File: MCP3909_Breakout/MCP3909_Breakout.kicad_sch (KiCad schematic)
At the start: 1 part

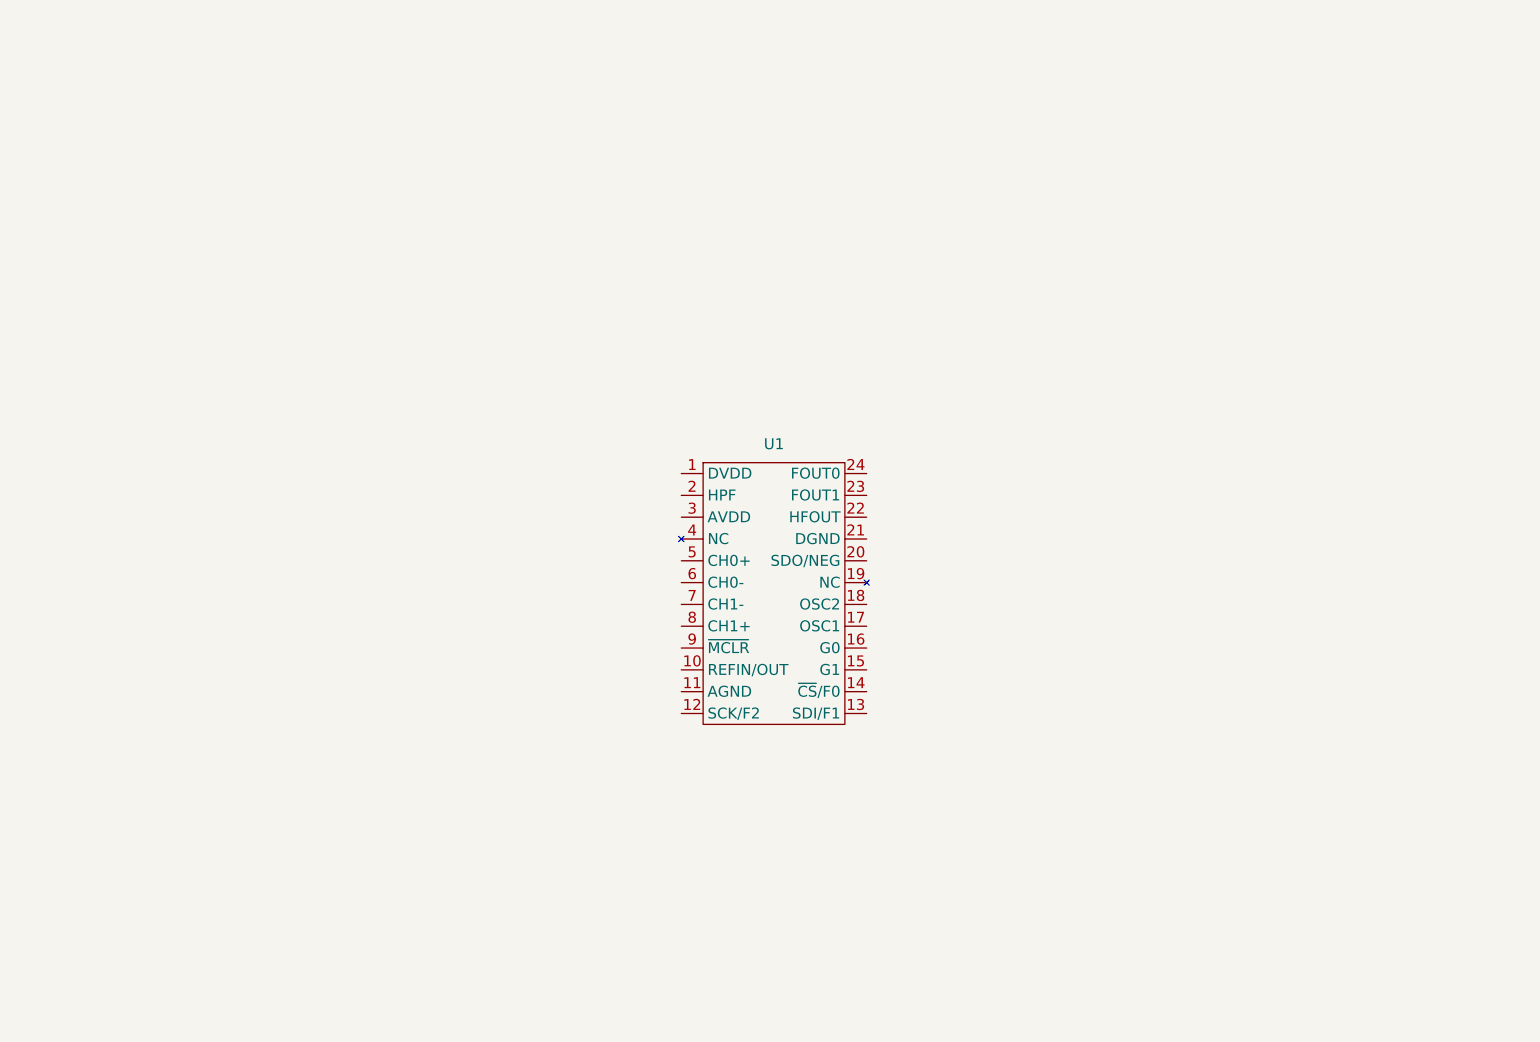
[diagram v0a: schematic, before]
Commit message: Complete wiring up most things
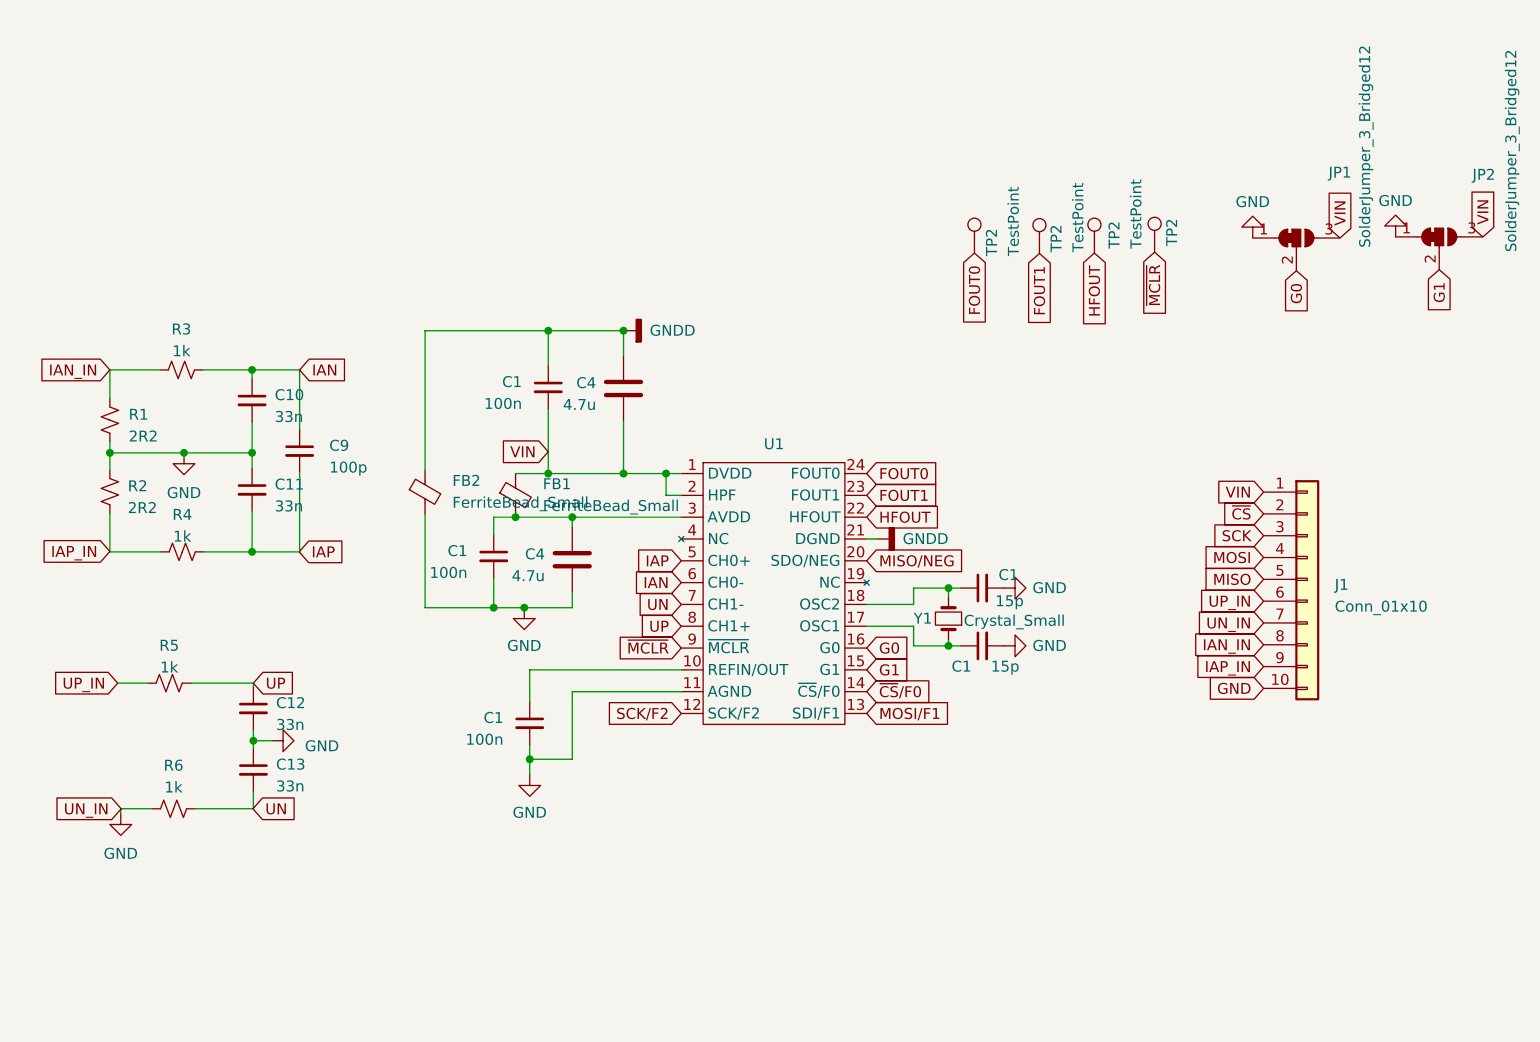
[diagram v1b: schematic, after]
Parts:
- added C1 (x2): 15p, Capacitor_SMD:C_0603_1608Metric, symbol Device:C_Small
- added C1 (x3): 100n, Capacitor_SMD:C_0603_1608Metric, symbol Device:C_Small
- added C10, C11, C12, C13: 33n, Capacitor_SMD:C_0603_1608Metric, symbol Device:C_Small
- added C4 (x2): 4.7u, Capacitor_SMD:C_0805_2012Metric, symbol Device:C
- added C9: 100p, Capacitor_SMD:C_0603_1608Metric, symbol Device:C_Small
- added FB1, FB2: FerriteBead_Small, Inductor_SMD:L_0603_1608Metric, symbol Device:FerriteBead_Small
- added J1: Conn_01x10, Connector_PinHeader_2.54mm:PinHeader_1x10_P2.54mm_Vertical, symbol Connector_Generic:Conn_01x10
- added JP1, JP2: SolderJumper_3_Bridged12, Jumper:SolderJumper-3_P1.3mm_Bridged12_RoundedPad1.0x1.5mm, symbol Jumper:SolderJumper_3_Bridged12
- added R1, R2: 2R2, Resistor_SMD:R_0603_1608Metric, symbol Device:R_Small_US
- added R3, R4, R5, R6: 1k, Resistor_SMD:R_0603_1608Metric, symbol Device:R_Small_US
- added TP2 (x4): TestPoint, TestPoint:TestPoint_Pad_1.5x1.5mm, symbol Connector:TestPoint
- added Y1: Crystal_Small, Crystal:Crystal_SMD_HC49-SD, symbol Device:Crystal_Small
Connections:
- net VIN: now reaches U1.1 (DVDD)
- net VIN: now also U1.2 (HPF), C1.2, C4.2, FB1.1, J1.1 (Pin_1), JP1.3 (B), JP2.3 (B)
- net at U1.10 (REFIN/OUT): now also C1.1
- net GND: now reaches U1.11 (AGND)
- net GND: now also C1.2, C1.2, C1.2, C1.2, C10.2, C11.1, C12.2, C13.1, C4.2, FB2.2, J1.10 (Pin_10), J1.7 (Pin_7), JP1.1 (A), JP2.1 (A), R1.2, R2.1, R6.1
- net SCK/F2: now reaches U1.12 (SCK/F2)
- net MOSI/F1: now reaches U1.13 (SDI/F1)
- net ~{CS}/F0: now reaches U1.14 (~{CS}/F0)
- net G1: now reaches U1.15 (G1)
- net G1: now also JP2.2 (C)
- net G0: now reaches U1.16 (G0)
- net G0: now also JP1.2 (C)
- net at U1.17 (OSC1): now also C1.1, Y1.1
- net at U1.18 (OSC2): now also C1.1, Y1.2
- net MISO/NEG: now reaches U1.20 (SDO/NEG)
- net GNDD: now reaches U1.21 (DGND)
- net GNDD: now also C1.1, C4.1, FB2.1
- net HFOUT: now reaches U1.22 (HFOUT)
- net HFOUT: now also TP2.1
- net FOUT1: now reaches U1.23 (FOUT1)
- net FOUT1: now also TP2.1
- net FOUT0: now reaches U1.24 (FOUT0)
- net FOUT0: now also TP2.1
- net at U1.3 (AVDD): now also C1.1, C4.1, FB1.2
- net IAP: now reaches U1.5 (CH0+)
- net IAP: now also C11.2, C9.2, R4.2
- net IAN: now reaches U1.6 (CH0-)
- net IAN: now also C10.1, C9.1, R3.2
- net UN: now reaches U1.7 (CH1-)
- net UN: now also C13.2, R6.2
- net UP: now reaches U1.8 (CH1+)
- net UP: now also C12.1, R5.2
- net ~{MCLR}: now reaches U1.9 (~{MCLR})
- net ~{MCLR}: now also TP2.1
- new net IAN_IN: J1.8 (Pin_8), R1.1, R3.1
- new net IAP_IN: J1.9 (Pin_9), R2.2, R4.1
- new net MISO: J1.5 (Pin_5)
- new net MOSI: J1.4 (Pin_4)
- new net SCK: J1.3 (Pin_3)
- new net UP_IN: J1.6 (Pin_6), R5.1
- new net ~{CS}: J1.2 (Pin_2)

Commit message: First go at place-n-route
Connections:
- net MISO is gone; now on net MISO/NEG: J1.5 (Pin_5)
- net MOSI is gone; now on net MOSI/F1: J1.4 (Pin_4)
- net SCK is gone; now on net SCK/F2: J1.3 (Pin_3)
- net ~{CS} is gone; now on net ~{CS}/F0: J1.2 (Pin_2)
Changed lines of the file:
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@@
     )
   )
-  (global_label "MOSI" (shape input) (at 210.947 86.868 180) (fields_autoplaced)
+  (global_label "MOSI{slash}F1" (shape input) (at 210.947 86.868 180) (fields_autoplaced)
     (effects (font (size 1.27 1.27)) (justify right))
-    (property "Intersheetrefs" "${INTERSHEET_REFS}" (at 203.3656 86.868 0)
+    (property "Intersheetrefs" "${INTERSHEET_REFS}" (at 199.737 86.868 0)
       (effects (font (size 1.27 1.27)) (justify right) hide)
     )
@@
     )
   )
-  (global_label "SCK" (shape input) (at 210.947 84.328 180) (fields_autoplaced)
+  (global_label "SCK{slash}F2" (shape input) (at 210.947 84.328 180) (fields_autoplaced)
     (effects (font (size 1.27 1.27)) (justify right))
-    (property "Intersheetrefs" "${INTERSHEET_REFS}" (at 204.2917 84.328 0)
+    (property "Intersheetrefs" "${INTERSHEET_REFS}" (at 200.5837 84.328 0)
       (effects (font (size 1.27 1.27)) (justify right) hide)
     )
@@
     )
   )
-  (global_label "MISO" (shape input) (at 210.947 89.408 180) (fields_autoplaced)
+  (global_label "MISO{slash}NEG" (shape input) (at 210.947 89.408 180) (fields_autoplaced)
     (effects (font (size 1.27 1.27)) (justify right))
-    (property "Intersheetrefs" "${INTERSHEET_REFS}" (at 203.3656 89.408 0)
+    (property "Intersheetrefs" "${INTERSHEET_REFS}" (at 198.2856 89.408 0)
       (effects (font (size 1.27 1.27)) (justify right) hide)
     )
@@
     )
   )
-  (global_label "~{CS}" (shape input) (at 210.947 81.788 180) (fields_autoplaced)
+  (global_label "~{CS}{slash}F0" (shape input) (at 210.947 81.788 180) (fields_autoplaced)
     (effects (font (size 1.27 1.27)) (justify right))
-    (property "Intersheetrefs" "${INTERSHEET_REFS}" (at 205.4823 81.788 0)
+    (property "Intersheetrefs" "${INTERSHEET_REFS}" (at 201.8537 81.788 0)
       (effects (font (size 1.27 1.27)) (justify right) hide)
     )

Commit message: Complete routing
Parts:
- added SYM1: Logo_Open_Hardware_Small, Symbol:OSHW-Logo2_9.8x8mm_SilkScreen, symbol Graphic:Logo_Open_Hardware_Small
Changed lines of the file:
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@@
+    )
+  )
+  (symbol (lib_id "Graphic:Logo_Open_Hardware_Small") (at 149.352 136.906 0) (unit 1)
+    (in_bom no) (on_board yes) (dnp no) (fields_autoplaced)
+    (property "Reference" "SYM1" (at 149.352 129.921 0)
+      (effects (font (size 1.27 1.27)) hide)
+    )
+    (property "Value" "Logo_Open_Hardware_Small" (at 149.352 142.621 0)
+      (effects (font (size 1.27 1.27)) hide)
+    )
+    (property "Footprint" "Symbol:OSHW-Logo2_9.8x8mm_SilkScreen" (at 149.352 136.906 0)
+      (effects (font (size 1.27 1.27)) hide)
+    )
+    (property "Datasheet" "~" (at 149.352 136.906 0)
+      (effects (font (size 1.27 1.27)) hide)
+    )
+    (property "Sim.Enable" "0" (at 149.352 136.906 0)
+      (effects (font (size 1.27 1.27)) hide)
+    )
+    (property "DNP" "..." (at 149.352 136.906 0)
+      (effects (font (size 1.27 1.27)) hide)
+    )
+    (property "MPN" "" (at 149.352 136.906 0)
+      (effects (font (size 1.27 1.27)) hide)
+    )
+    (instances
+      (project "V9381_Breakout"
+        (path "/891e2995-ecf8-4e0a-82a0-40782119b9b2"
+          (reference "SYM1") (unit 1)
+        )
+      )
+      (project "MCP3909_Breakout"
+        (path "/899a7509-31b8-4e59-b332-cc9b02b5ed06"
+          (reference "SYM1") (unit 1)
+        )
+      )
+      (project "V9360_Breakout"
+        (path "/f6ffeb9c-2174-49f8-b838-c33315c45e1a"
+          (reference "SYM1") (unit 1)
+        )
+      )
     )
   )

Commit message: Produce fabrication outputs
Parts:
- FB1, FB2: MPN (none) -> BLM03AG100SN1D
- U1: value ~ -> MCP3909; MPN (none) -> MCP3909
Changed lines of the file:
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@@
+      (effects (font (size 1.27 1.27)) hide)
+    )
+    (property "MPN" "BLM03AG100SN1D" (at 123.825 79.629 0)
       (effects (font (size 1.27 1.27)) hide)
     )
@@
       (effects (font (size 1.27 1.27)) hide)
     )
+    (property "MPN" "BLM03AG100SN1D" (at 113.284 79.248 0)
+      (effects (font (size 1.27 1.27)) hide)
+    )
     (pin "1")
     (pin "2")
@@
       (effects (font (size 1.27 1.27)))
     )
-    (property "Value" "~" (at 154.559 74.549 0)
+    (property "Value" "MCP3909" (at 154.559 74.549 0)
       (effects (font (size 1.27 1.27)))
     )
@@
       (effects (font (size 1.27 1.27)) hide)
     )
+    (property "MPN" "MCP3909" (at 154.559 74.549 0)
+      (effects (font (size 1.27 1.27)) hide)
+    )
